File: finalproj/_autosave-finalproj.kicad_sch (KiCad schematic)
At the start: 46 parts, among them J1 RPI UART, J2 Conn_01x02, J3 Motor_Controller_Connector, J4 DC_Motor_Power_Connector, J5 Stepper_Motor_Controller, J6 Step_Motor_Power_Connector, J7 LIDAR_Connector, J8 Programmer_Conn, U1 STM32F767ZITx, U2 LM1085-12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

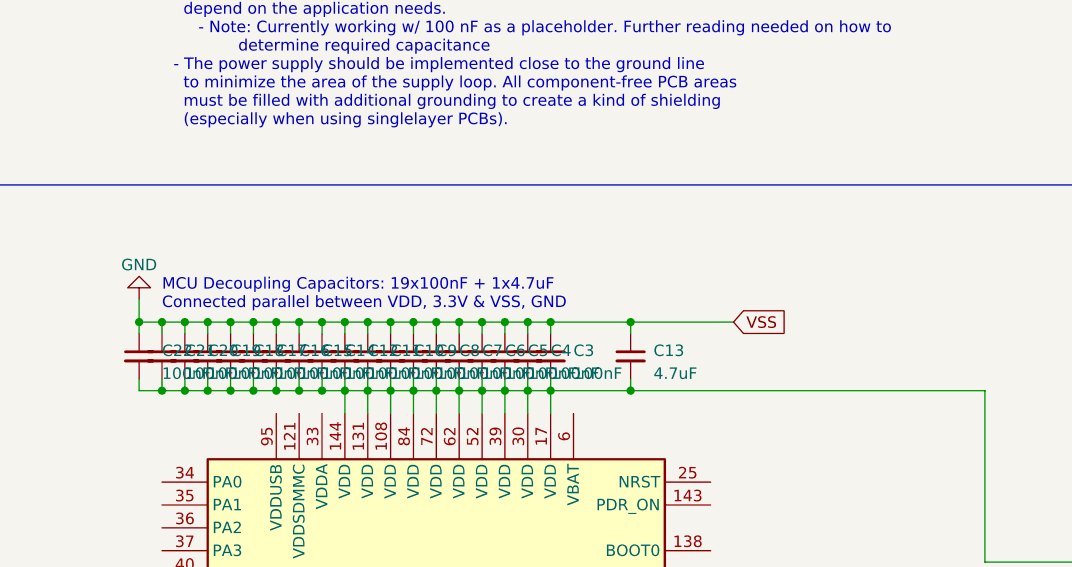
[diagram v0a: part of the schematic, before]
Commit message: MCU power supply done
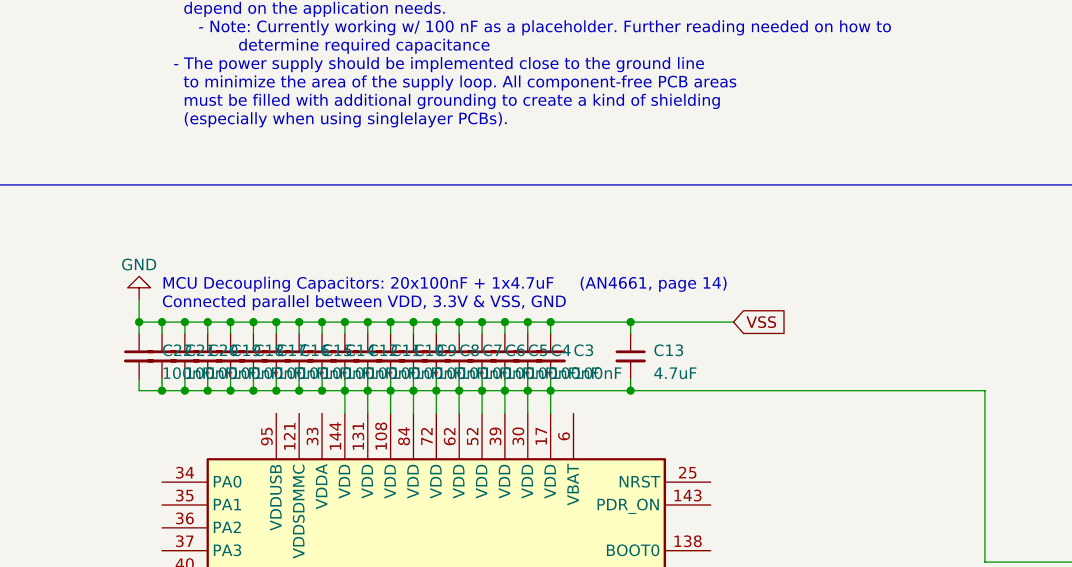
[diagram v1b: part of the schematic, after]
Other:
- note added: "MCU Decoupling Capacitors: 20x100nF + 1x4.7uF (AN4661, page 14) Connected parallel between VDD, 3.3V & VSS, GND"
- note removed: "MCU Decoupling Capacitors: 19x100nF + 1x4.7uF Connected parallel between VDD, 3.3V & VSS, GND"
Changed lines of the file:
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@@
     (stroke (width 0) (type default))
   )
-  (text "MCU Decoupling Capacitors: 19x100nF + 1x4.7uF \nConnected parallel between VDD, 3.3V & VSS, GND"
+  (text "MCU Decoupling Capacitors: 20x100nF + 1x4.7uF     (AN4661, page 14)\nConnected parallel between VDD, 3.3V & VSS, GND"
     (at 236.22 27.94 0)
     (effects (font (size 1.27 1.27)) (justify left bottom))
